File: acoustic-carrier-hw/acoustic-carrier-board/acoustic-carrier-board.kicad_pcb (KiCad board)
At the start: 6 copper layers, 99 x 97 mm, 363 parts, among them IC1 ECP5-BGA256, IC1101 MT41K256M16TW-107_P, J1001 BWU.FL-IPEX1, J1002 BWU.FL-IPEX1, J1003 BWU.FL-IPEX1, J1005 BWU.FL-IPEX1, J1006 BWU.FL-IPEX1, J1007 8P8C_Shielded, J1008 BWU.FL-IPEX1, J1009 BWU.FL-IPEX1, J1010 BWU.FL-IPEX1, J1201 HR911130A, J201 Conn_02x06_Odd_Even, J701 Conn_02x03_Odd_Even, J702 PMOD_JTAG, J703 PMOD_SPI, J704 PMOD_GPIO, J801 TYPE-C-31-M-12, J903 Conn_02x06_Odd_Even, Q201 AO3401A, U1001 MS9280, U1002 THS4521IDGK, U1003 DGQ2788AEN-T1-GE4, U1004 LMV321, U1005 TL432DBZ, U1201 KSZ9031RN, U201 TPS2121RUX, U202 TLV62569DBV, U203 TLV62569DBV, U204 TLV62569DBV, U205 TLV62569DBV, U206 OPA376xxDBV, U701 W25Q128JVS, U702 W25Q128JVS, U801 USB3300-EZK, U802 LMV321, Y1201 25MHz, Y401 Crystal Oscillator, Y801 Crystal_GND24_Small

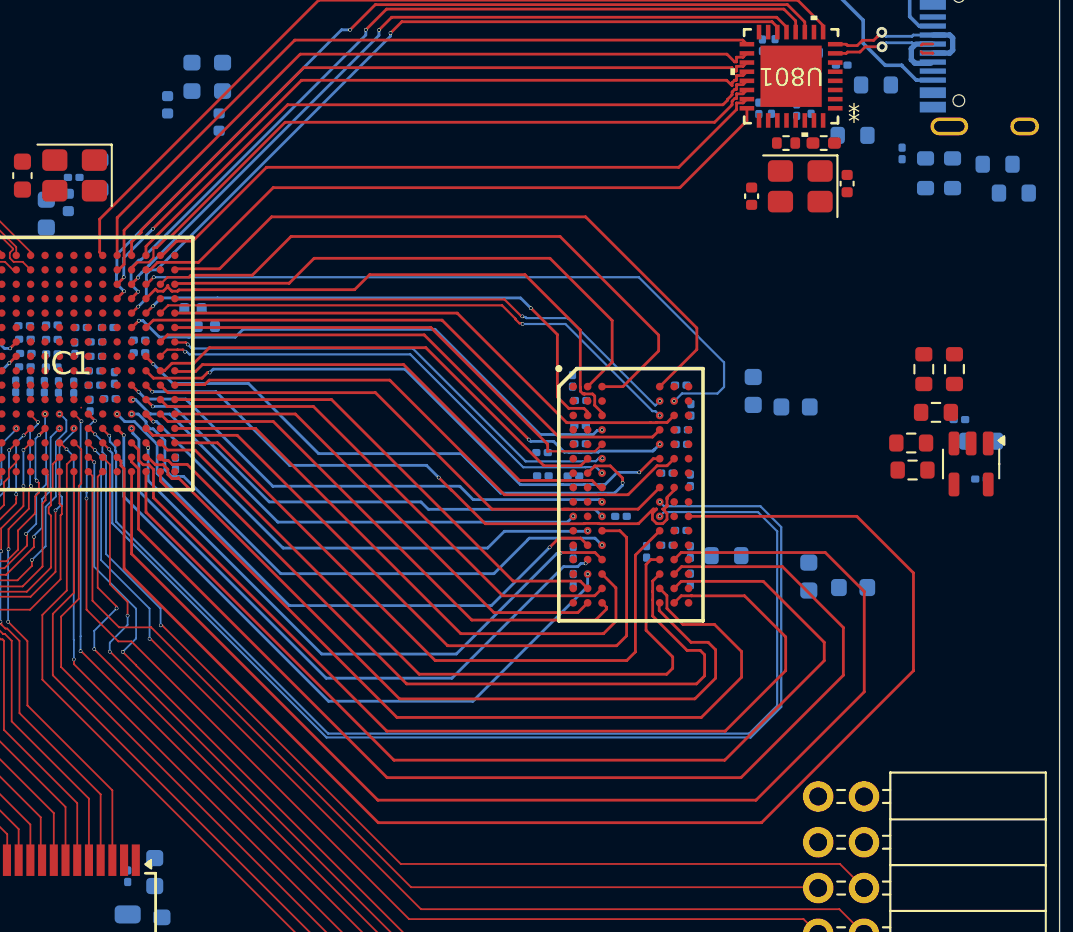
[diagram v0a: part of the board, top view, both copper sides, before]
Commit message: [carrier] Matched address bus to 60 mm (nextt) match dq groups to 60 mm
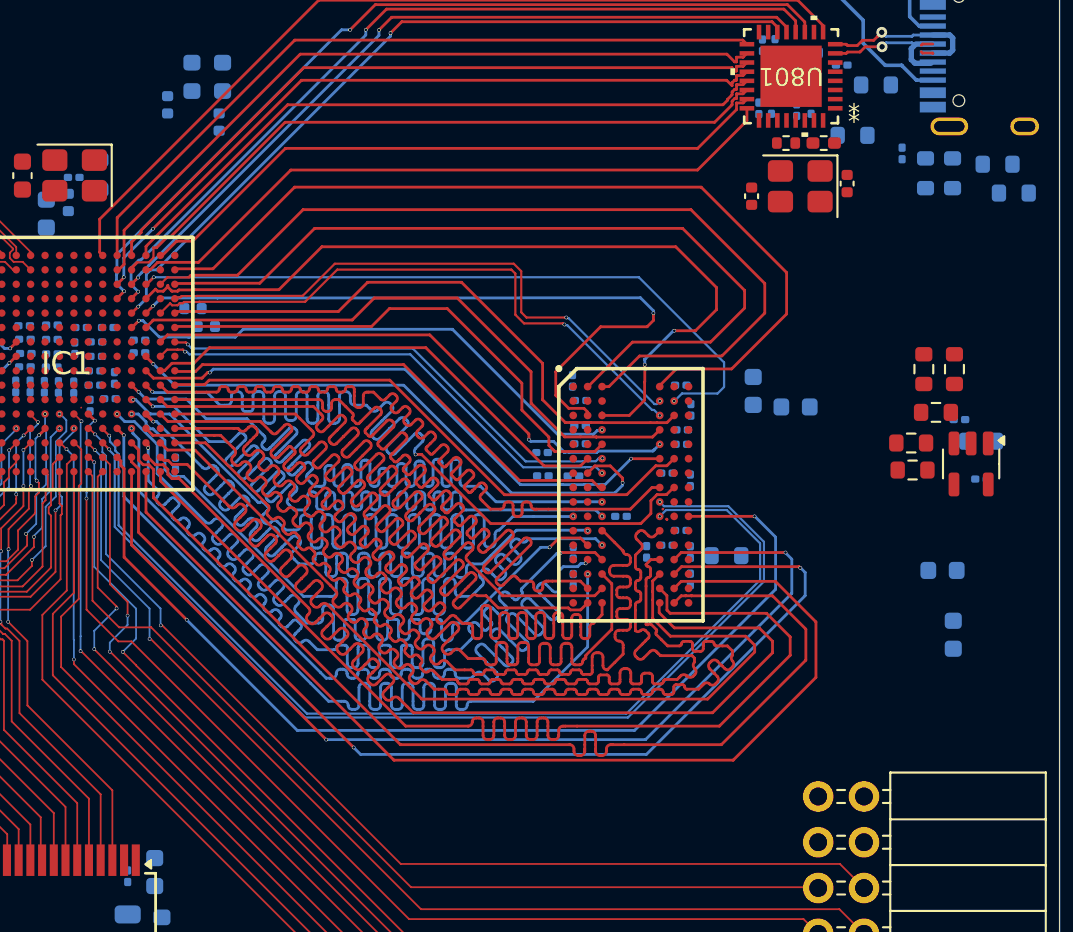
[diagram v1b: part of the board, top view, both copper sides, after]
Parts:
- moved C1113 8.64 mm to (138.1, 102.9)
- moved L1102 5.05 mm to (137.5, 99.3)
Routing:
- net /DDR3/DDR3.A13: track 30.2 -> 69.5 mm
- net /DDR3/DDR3.RESET#: track 27.7 -> 59.5 mm
- net /DDR3/DDR3.A7: track 27.3 -> 58.7 mm
- net /DDR3/DDR3.ODT: track 27.4 -> 57.7 mm
- net /DDR3/DDR3.A9: track 29.2 -> 59.0 mm
- net /DDR3/DDR3.CAS#: track 28.0 -> 57.2 mm
- net /DDR3/DDR3.CS#: track 28.0 -> 55.8 mm
- net /DDR3/DDR3.RAS#: track 28.8 -> 55.9 mm
- net /DDR3/DDR3.A2: track 32.4 -> 58.6 mm
- net /DDR3/DDR3.BA2: track 31.8 -> 56.4 mm
- net /DDR3/DDR3.BA0: track 33.2 -> 56.2 mm
- net /DDR3/DDR3.A0: track 33.9 -> 55.8 mm
- net /DDR3/DDR3.DQ5: track 35.7 -> 57.2 mm
- net /DDR3/DDR3.A3: track 35.7 -> 57.1 mm
- net /DDR3/DDR3.CKE: track 78.7 -> 57.3 mm, vias 0 -> 2
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
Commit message: [carrier] Finished LPDDR3 length-matching (next) finetune clock and spatial lpddr3, finetune rgmii, usb, ..
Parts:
- moved C406 16.0 mm to (87.8, 72.5)
- moved C1107 3.80 mm to (126.6, 93.2)
- moved L1101 3.80 mm to (129.0, 94.0)
- moved C603 2.37 mm to (97.1, 82.7)
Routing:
- net /DDR3/DDR3.DQ4: track 26.8 -> 59.7 mm
- net /DDR3/DDR3.DQ2: track 27.1 -> 59.7 mm
- net /DDR3/DDR3.DQ0: track 28.8 -> 59.7 mm
- net /DDR3/DDR3.LDQS-: track 27.7 -> 57.4 mm
- net /DDR3/DDR3.LDQS+: track 26.7 -> 56.3 mm
- net /DDR3/DDR3.DQ3: track 31.3 -> 59.4 mm
- net /DDR3/DDR3.LDM: track 31.2 -> 58.3 mm
- net /DDR3/DDR3.UDM: track 29.3 -> 56.5 mm
- net /DDR3/DDR3.DQ1: track 32.1 -> 56.7 mm
- net /DDR3/DDR3.DQ6: track 32.6 -> 56.6 mm
- net /DDR3/DDR3.UDQS-: track 33.5 -> 56.9 mm
- net /DDR3/DDR3.UDQS+: track 32.5 -> 55.6 mm
- net /DDR3/DDR3.DQ10: track 33.6 -> 56.5 mm, vias 0 -> 2
- net /DDR3/DDR3.DQ8: track 33.6 -> 56.4 mm, vias 0 -> 2
- net /DDR3/DDR3.DQ14: track 38.7 -> 57.1 mm
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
